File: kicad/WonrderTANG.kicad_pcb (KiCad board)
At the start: 2 copper layers, 101.6 x 90.2 mm, 31 parts, among them CON1 MSX-CONNECTOR, J1 Conn_02x01, J2 AudioJack3, J3 Conn_02x01, Q1 2N3904, U1 SN74LVC245AN, U2 SN74LVC245AN, U3 SN74LVC245AN, U4 SN74LVC245AN, U5 Tang_Nano_20k, U6 SN74LVC245AN

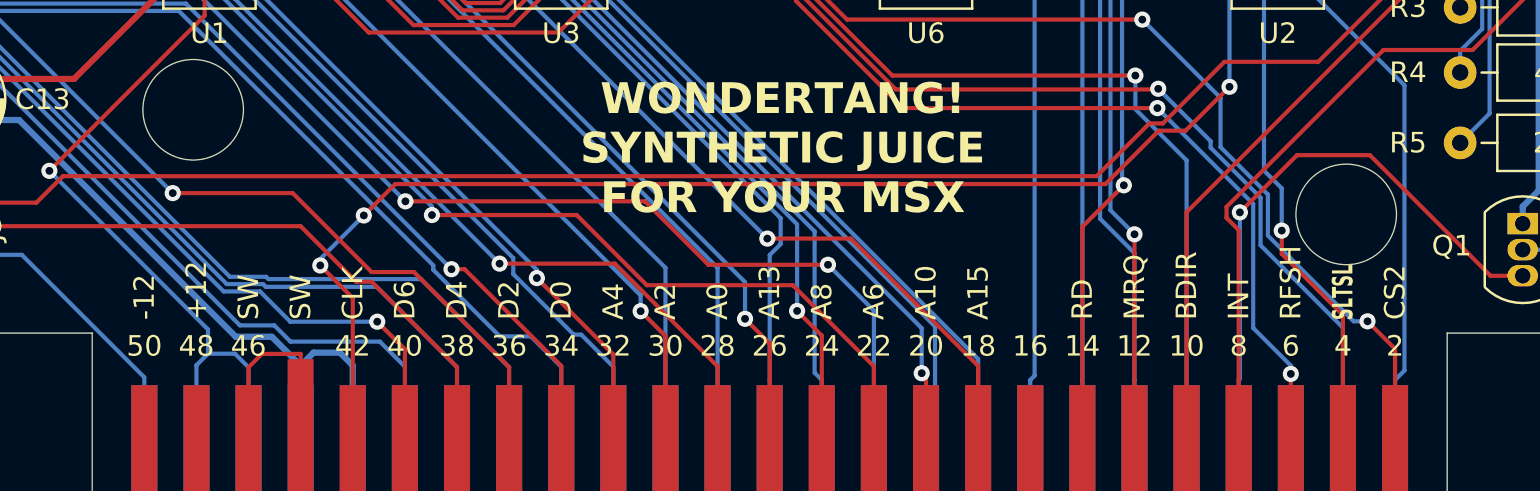
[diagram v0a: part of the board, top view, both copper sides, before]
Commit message: [kicad] Silkscreen updates for cartridge pads
Mark active low signals BDIR,CS1,CS2,CS12,INT,IRQ,M1,MRQ,RD,RFSH,RST,SLTSL,WAIT,WR with a bar above them.
Add voltage suffix V to +5, +12 and -12 signals.
Add pad number to pad 43.
Add pad number to pad 44.
Name each SW pad with its own names SW1 and SW2.
Rename BDIR to BUSDIR.
Rename CLK to CLOCK.
Rename RST to RESET.
Rename SND to SOUNDIN.

Signed-off-by: Albert Herranz <albert_herranz@yahoo.es>
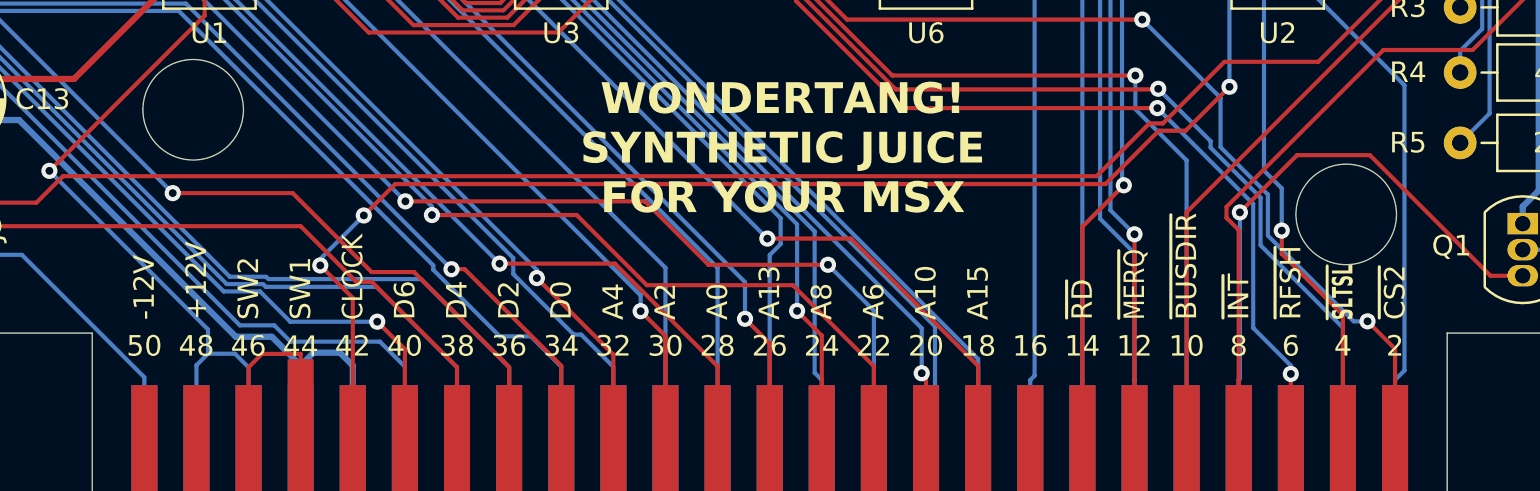
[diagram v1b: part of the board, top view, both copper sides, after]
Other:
- board text added: "+12V"
- board text added: "+5V"
- board text added: "-12V"
- board text added: "43"
- board text added: "44"
- board text added: "CLOCK"
- board text added: "SOUNDIN"
- board text added: "SW1"
- board text added: "SW2"
- board text added: "~{BUSDIR}"
- board text added: "~{CS12}"
- board text added: "~{CS1}"
- board text added: "~{CS2}"
- board text added: "~{INT}"
- board text added: "~{IORQ}"
- board text added: "~{M1}"
- board text added: "~{MERQ}"
- board text added: "~{RD}"
- board text added: "~{RESET}"
- board text added: "~{RFSH}"
- board text added: "~{SLTSL}"
- board text added: "~{WAIT}"
- board text added: "~{WR}"
- board text removed: "+12"
- board text removed: "+5"
- board text removed: "-12"
- board text removed: "BDIR"
- board text removed: "CLK"
- board text removed: "CS1"
- board text removed: "CS12"
- board text removed: "CS2"
- board text removed: "INT"
- board text removed: "IRQ"
- board text removed: "M1"
- board text removed: "MRQ"
- board text removed: "RD"
- board text removed: "RFSH"
- board text removed: "RST"
- board text removed: "SLTSL"
- board text removed: "SND"
- board text removed: "SW"
- board text removed: "WAIT"
- board text removed: "WR"
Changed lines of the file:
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@@
     (effects (font (size 1 1) (thickness 0.15)) (justify mirror))
   )
-  (gr_text "M1" (at 132.08 132.715 -90) (layer "B.SilkS")
+  (gr_text "~{M1}" (at 132.08 132.715 270) (layer "B.SilkS")
     (effects (font (size 1 1) (thickness 0.15)) (justify left mirror))
   )
@@
     (effects (font (size 1 1) (thickness 0.15)) (justify left mirror))
   )
-  (gr_text "+5" (at 83.82 132.715 -90) (layer "B.SilkS")
+  (gr_text "+5V" (at 83.82 132.715 270) (layer "B.SilkS")
     (effects (font (size 1 1) (thickness 0.15)) (justify left mirror))
   )
@@
     (effects (font (size 1 1) (thickness 0.15)) (justify mirror))
   )
-  (gr_text "SND" (at 81.28 132.715 -90) (layer "B.SilkS")
+  (gr_text "SOUNDIN" (at 81.28 132.715 270) (layer "B.SilkS")
     (effects (font (size 1 1) (thickness 0.15)) (justify left mirror))
   )
@@
     (effects (font (size 1 1) (thickness 0.15)) (justify left mirror))
   )
-  (gr_text "RST" (at 124.46 132.715 -90) (layer "B.SilkS")
-    (effects (font (size 1 1) (thickness 0.15)) (justify left mirror))
-  )
-  (gr_text "CS12" (at 139.7 132.715 -90) (layer "B.SilkS")
+  (gr_text "~{RESET}" (at 124.46 132.715 270) (layer "B.SilkS")
+    (effects (font (size 1 1) (thickness 0.15)) (justify left mirror))
+  )
+  (gr_text "~{CS12}" (at 139.7 132.715 270) (layer "B.SilkS")
     (effects (font (size 1 0.65) (thickness 0.145)) (justify left mirror))
   )
@@
     (effects (font (size 1 1) (thickness 0.15)) (justify mirror))
   )
-  (gr_text "WR" (at 127 132.715 -90) (layer "B.SilkS")
+  (gr_text "~{WR}" (at 127 132.715 270) (layer "B.SilkS")
     (effects (font (size 1 1) (thickness 0.15)) (justify left mirror))
   )
@@
     (effects (font (size 1 1) (thickness 0.15)) (justify left mirror))
   )
-  (gr_text "CS1" (at 142.24 132.715 -90) (layer "B.SilkS")
+  (gr_text "~{CS1}" (at 142.24 132.715 270) (layer "B.SilkS")
     (effects (font (size 1 1) (thickness 0.15)) (justify left mirror))
   )
@@
     (effects (font (size 1 1) (thickness 0.15)) (justify mirror))
   )
-  (gr_text "IRQ" (at 129.54 132.715 -90) (layer "B.SilkS")
+  (gr_text "~{IORQ}" (at 129.54 132.715 270) (layer "B.SilkS")
     (effects (font (size 1 1) (thickness 0.15)) (justify left mirror))
   )
@@
     (effects (font (size 1 1) (thickness 0.15)) (justify mirror))
   )
+  (gr_text "43" (at 88.9 134) (layer "B.SilkS")
+    (effects (font (size 1 1) (thickness 0.15)) (justify mirror))
+  )
   (gr_text "37" (at 96.52 133.985) (layer "B.SilkS")
     (effects (font (size 1 1) (thickness 0.15)) (justify mirror))
@@
     (effects (font (size 1 1) (thickness 0.15)) (justify left mirror))
   )
-  (gr_text "WAIT" (at 134.62 132.715 -90) (layer "B.SilkS")
+  (gr_text "~{WAIT}" (at 134.62 132.715 270) (layer "B.SilkS")
     (effects (font (size 1 1) (thickness 0.15)) (justify left mirror))
   )
@@
     (effects (font (size 1 1) (thickness 0.15)) (justify mirror))
   )
-  (gr_text "+5" (at 86.36 132.715 -90) (layer "B.SilkS")
+  (gr_text "+5V" (at 86.36 132.715 270) (layer "B.SilkS")
     (effects (font (size 1 1) (thickness 0.15)) (justify left mirror))
   )
@@
     (effects (font (size 1 1) (thickness 0.15)))
   )
-  (gr_text "+12" (at 83.82 132.715 90) (layer "F.SilkS")
+  (gr_text "+12V" (at 83.82 132.715 90) (layer "F.SilkS")
     (effects (font (size 1 1) (thickness 0.15)) (justify left))
   )
@@
     (effects (font (size 1 1) (thickness 0.15)))
   )
-  (gr_text "SW" (at 86.36 132.715 90) (layer "F.SilkS")
+  (gr_text "SW2" (at 86.36 132.715 90) (layer "F.SilkS")
     (effects (font (size 1 1) (thickness 0.15)) (justify left))
   )
@@
     (effects (font (size 1 1) (thickness 0.15)) (justify left))
   )
-  (gr_text "-12" (at 81.28 132.715 90) (layer "F.SilkS")
+  (gr_text "-12V" (at 81.28 132.715 90) (layer "F.SilkS")
     (effects (font (size 1 1) (thickness 0.15)) (justify left))
   )
@@
     (effects (font (size 1 1) (thickness 0.15)))
   )
-  (gr_text "CS2" (at 142.24 132.715 90) (layer "F.SilkS")
+  (gr_text "~{CS2}" (at 142.24 132.715 90) (layer "F.SilkS")
     (effects (font (size 1 1) (thickness 0.15)) (justify left))
   )
@@
     (effects (font (size 1 1) (thickness 0.15)) (justify left))
   )
-  (gr_text "CLK" (at 91.44 132.715 90) (layer "F.SilkS")
-    (effects (font (size 1 1) (thickness 0.15)) (justify left))
+  (gr_text "CLOCK" (at 91.44 132.715 90) (layer "F.SilkS")
+    (effects (font (size 1 0.9) (thickness 0.15)) (justify left))
   )
   (gr_text "A10" (at 119.38 132.715 90) (layer "F.SilkS")
     (effects (font (size 1 1) (thickness 0.15)) (justify left))
   )
+  (gr_text "44" (at 88.9 134) (layer "F.SilkS")
+    (effects (font (size 1 1) (thickness 0.15)))
+  )
   (gr_text "24" (at 114.3 133.985) (layer "F.SilkS")
     (effects (font (size 1 1) (thickness 0.15)))
@@
     (effects (font (size 1 1) (thickness 0.15)))
   )
-  (gr_text "BDIR" (at 132.08 132.715 90) (layer "F.SilkS")
+  (gr_text "~{BUSDIR}" (at 132.08 132.715 90) (layer "F.SilkS")
     (effects (font (size 1 1) (thickness 0.15)) (justify left))
   )
@@
     (effects (font (size 1 1) (thickness 0.15)))
   )
-  (gr_text "RD" (at 127 132.715 90) (layer "F.SilkS")
+  (gr_text "~{RD}" (at 127 132.715 90) (layer "F.SilkS")
     (effects (font (size 1 1) (thickness 0.15)) (justify left))
   )
@@
     (effects (font (size 1 1) (thickness 0.15)))
   )
-  (gr_text "INT" (at 134.62 132.715 90) (layer "F.SilkS")
+  (gr_text "~{INT}" (at 134.62 132.715 90) (layer "F.SilkS")
     (effects (font (size 1 1) (thickness 0.15)) (justify left))
   )
@@
     (effects (font (size 1.5 1.5) (thickness 0.3) bold) (justify left bottom))
   )
-  (gr_text "SW" (at 88.9 132.715 90) (layer "F.SilkS")
+  (gr_text "SW1" (at 88.9 132.715 90) (layer "F.SilkS")
     (effects (font (size 1 1) (thickness 0.15)) (justify left))
   )
@@
     (effects (font (size 1 1) (thickness 0.15)) (justify left))
   )
-  (gr_text "RFSH" (at 137.16 132.715 90) (layer "F.SilkS")
+  (gr_text "~{RFSH}" (at 137.16 132.715 90) (layer "F.SilkS")
     (effects (font (size 1 1) (thickness 0.15)) (justify left))
   )
@@
     (effects (font (size 1.5 1.5) (thickness 0.3) bold) (justify bottom))
   )
-  (gr_text "SLTSL" (at 139.7 132.715 90) (layer "F.SilkS")
+  (gr_text "~{SLTSL}" (at 139.7 132.715 90) (layer "F.SilkS")
     (effects (font (size 1 0.58) (thickness 0.145) bold) (justify left))
   )
@@
     (effects (font (size 1 1) (thickness 0.15)) (justify left))
   )
-  (gr_text "MRQ" (at 129.54 132.715 90) (layer "F.SilkS")
-    (effects (font (size 1 1) (thickness 0.15)) (justify left))
+  (gr_text "~{MERQ}" (at 129.54 132.715 90) (layer "F.SilkS")
+    (effects (font (size 1 0.85) (thickness 0.15)) (justify left))
   )
   (segment (start 88.265 93.345) (end 89.7717 93.345) (width 0.3048) (layer "F.Cu") (net 1))

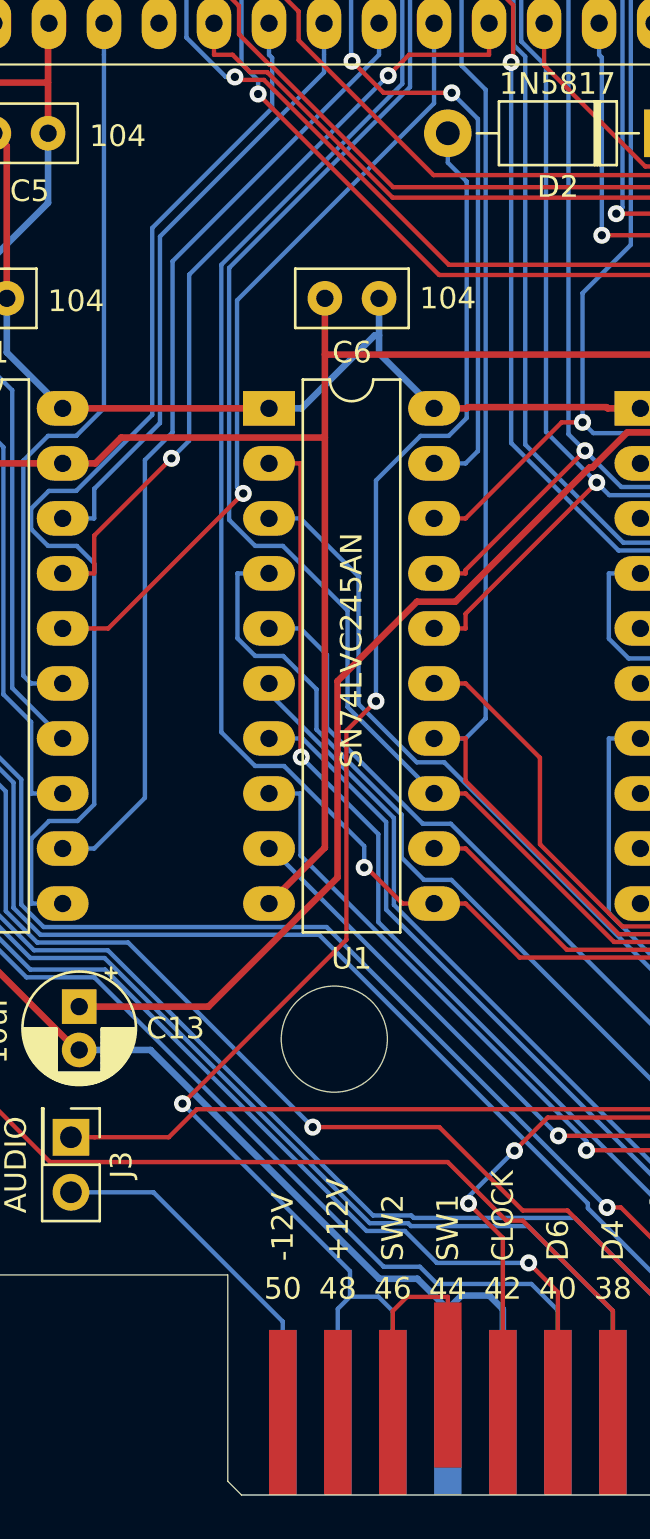
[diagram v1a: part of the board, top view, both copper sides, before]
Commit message: [kicad] Fix /CART_5V net width
Update the PCB to bring /CART_5V in sync with the schematic.
Apply the power netclass width to /CART_5V as it is currently using a
smaller width than the rest of power nets (from the cartridge pads to the
D2 diode).
Add clearance when needed to account for the increase in net width.

Signed-off-by: Albert Herranz <albert_herranz@yahoo.es>
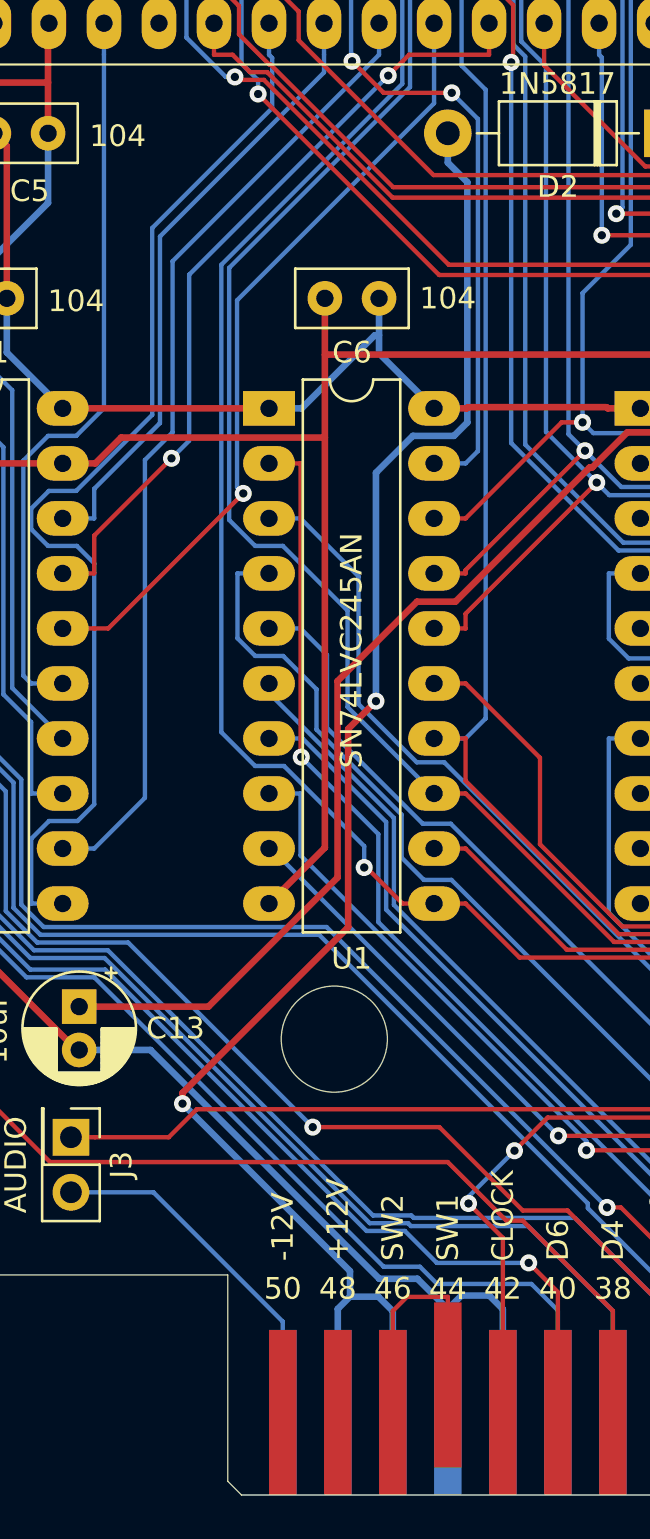
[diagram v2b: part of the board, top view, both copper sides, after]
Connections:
- net Net-(CON1-5V@1) renamed /CART_5V
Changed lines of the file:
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@@
   (net 75 "WAIT_33")
   (net 76 "SOUNDIN")
-  (net 77 "Net-(CON1-5V@1)")
+  (net 77 "/CART_5V")
   (net 78 "JP")
   (net 79 "DATADIR")
@@
       (net 3 "+5V") (pinfunction "K") (pintype "passive"))
     (pad "2" thru_hole oval (at 10.16 0 180) (size 2.2 2.2) (drill 1.1) (layers "*.Cu" "*.Mask")
-      (net 77 "Net-(CON1-5V@1)") (pinfunction "A") (pintype "passive"))
+      (net 77 "/CART_5V") (pinfunction "A") (pintype "passive"))
     (model "${KICAD6_3DMODEL_DIR}/Diode_THT.3dshapes/D_DO-41_SOD81_P10.16mm_Horizontal.wrl"
       (offset (xyz 0 0 0))
@@
       (net 6 "Net-(CON1-SW1)") (pinfunction "SW1") (pintype "bidirectional"))
     (pad "45" connect rect (at -25.4 0.635) (size 1.27 7.62) (layers "B.Cu" "B.Paste" "B.Mask")
-      (net 77 "Net-(CON1-5V@1)") (pinfunction "5V@1") (pintype "bidirectional"))
+      (net 77 "/CART_5V") (pinfunction "5V@1") (pintype "bidirectional"))
     (pad "46" connect rect (at -25.4 0.635) (size 1.27 7.62) (layers "F.Cu" "F.Paste" "F.Mask")
       (net 6 "Net-(CON1-SW1)") (pinfunction "SW2") (pintype "bidirectional"))
     (pad "47" connect rect (at -27.94 0.635) (size 1.27 7.62) (layers "B.Cu" "B.Paste" "B.Mask")
-      (net 77 "Net-(CON1-5V@1)") (pinfunction "5V@2") (pintype "bidirectional"))
+      (net 77 "/CART_5V") (pinfunction "5V@2") (pintype "bidirectional"))
     (pad "48" connect rect (at -27.94 0.635) (size 1.27 7.62) (layers "F.Cu" "F.Paste" "F.Mask")
       (net 8 "unconnected-(CON1-+12-Pad48)") (pinfunction "+12") (pintype "bidirectional+no_connect"))
@@
   (segment (start 81.28 139.7) (end 81.28 135.5056) (width 0.2032) (layer "B.Cu") (net 76))
   (segment (start 81.28 135.5056) (end 75.3094 129.535) (width 0.2032) (layer "B.Cu") (net 76))
-  (segment (start 84.2185 117.8762) (end 84.2185 108.2276) (width 0.2032) (layer "F.Cu") (net 77))
-  (segment (start 84.2185 108.2276) (end 85.5825 106.8636) (width 0.2032) (layer "F.Cu") (net 77))
-  (segment (start 76.6522 125.4425) (end 84.2185 117.8762) (width 0.2032) (layer "F.Cu") (net 77))
+  (segment (start 84.3 108.1461) (end 85.5825 106.8636) (width 0.3048) (layer "F.Cu") (net 77))
+  (segment (start 76.6522 124.9478) (end 84.3 117.3) (width 0.3048) (layer "F.Cu") (net 77))
+  (segment (start 84.3 117.3) (end 84.3 108.1461) (width 0.3048) (layer "F.Cu") (net 77))
+  (segment (start 76.6522 125.4425) (end 76.6522 124.9478) (width 0.3048) (layer "F.Cu") (net 77))
   (via (at 85.5825 106.8636) (size 0.7874) (drill 0.381) (layers "F.Cu" "B.Cu") (net 77))
   (via (at 76.6522 125.4425) (size 0.7874) (drill 0.381) (layers "F.Cu" "B.Cu") (net 77))
-  (segment (start 89.7709 82.8718) (end 89.7709 93.7876) (width 0.2032) (layer "B.Cu") (net 77))
-  (segment (start 84.3841 133.1744) (end 76.6522 125.4425) (width 0.2032) (layer "B.Cu") (net 77))
-  (segment (start 85.6948 134.355) (end 86.36 135.0202) (width 0.2032) (layer "B.Cu") (net 77))
-  (segment (start 85.5825 96.674) (end 85.5825 106.8636) (width 0.2032) (layer "B.Cu") (net 77))
-  (segment (start 84.3841 134.355) (end 84.3841 133.1744) (width 0.2032) (layer "B.Cu") (net 77))
-  (segment (start 86.36 135.0202) (end 86.36 139.7) (width 0.2032) (layer "B.Cu") (net 77))
-  (segment (start 88.9435 94.615) (end 87.6415 94.615) (width 0.2032) (layer "B.Cu") (net 77))
-  (segment (start 87.6415 94.615) (end 85.5825 96.674) (width 0.2032) (layer "B.Cu") (net 77))
-  (segment (start 88.9 80.645) (end 88.9 82.0009) (width 0.2032) (layer "B.Cu") (net 77))
-  (segment (start 88.9 82.0009) (end 89.7709 82.8718) (width 0.2032) (layer "B.Cu") (net 77))
-  (segment (start 89.7709 93.7876) (end 88.9435 94.615) (width 0.2032) (layer "B.Cu") (net 77))
-  (segment (start 84.3841 134.355) (end 85.6948 134.355) (width 0.2032) (layer "B.Cu") (net 77))
-  (segment (start 83.82 139.7) (end 83.82 134.9191) (width 0.2032) (layer "B.Cu") (net 77))
-  (segment (start 83.82 134.9191) (end 84.3841 134.355) (width 0.2032) (layer "B.Cu") (net 77))
+  (segment (start 87.285 94.615) (end 85.5825 96.3175) (width 0.3048) (layer "B.Cu") (net 77))
+  (segment (start 89.8 94) (end 89.185 94.615) (width 0.3048) (layer "B.Cu") (net 77))
+  (segment (start 89.185 94.615) (end 87.285 94.615) (width 0.3048) (layer "B.Cu") (net 77))
+  (segment (start 84.3841 133.1744) (end 76.6522 125.4425) (width 0.3048) (layer "B.Cu") (net 77))
+  (segment (start 85.6948 134.355) (end 86.36 135.0202) (width 0.3048) (layer "B.Cu") (net 77))
+  (segment (start 84.3841 134.355) (end 84.3841 133.1744) (width 0.3048) (layer "B.Cu") (net 77))
+  (segment (start 86.36 135.0202) (end 86.36 139.7) (width 0.3048) (layer "B.Cu") (net 77))
+  (segment (start 84.3841 134.355) (end 85.6948 134.355) (width 0.3048) (layer "B.Cu") (net 77))
+  (segment (start 88.9 82.0009) (end 89.8 82.9009) (width 0.3048) (layer "B.Cu") (net 77))
+  (segment (start 85.5825 96.3175) (end 85.5825 106.8636) (width 0.3048) (layer "B.Cu") (net 77))
+  (segment (start 83.82 139.7) (end 83.82 134.9191) (width 0.3048) (layer "B.Cu") (net 77))
+  (segment (start 89.8 82.9009) (end 89.8 94) (width 0.3048) (layer "B.Cu") (net 77))
+  (segment (start 83.82 134.9191) (end 84.3841 134.355) (width 0.3048) (layer "B.Cu") (net 77))
+  (segment (start 88.9 80.645) (end 88.9 82.0009) (width 0.3048) (layer "B.Cu") (net 77))
   (segment (start 60.325 74.1091) (end 60.7191 73.715) (width 0.2032) (layer "F.Cu") (net 78))
   (segment (start 115.7021 82.577) (end 116.9991 81.28) (width 0.2032) (layer "F.Cu") (net 78))
